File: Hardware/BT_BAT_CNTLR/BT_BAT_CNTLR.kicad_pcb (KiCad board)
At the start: 2 copper layers, 145 x 60 mm, 10 parts, among them J1 Barrel_Jack_Switch

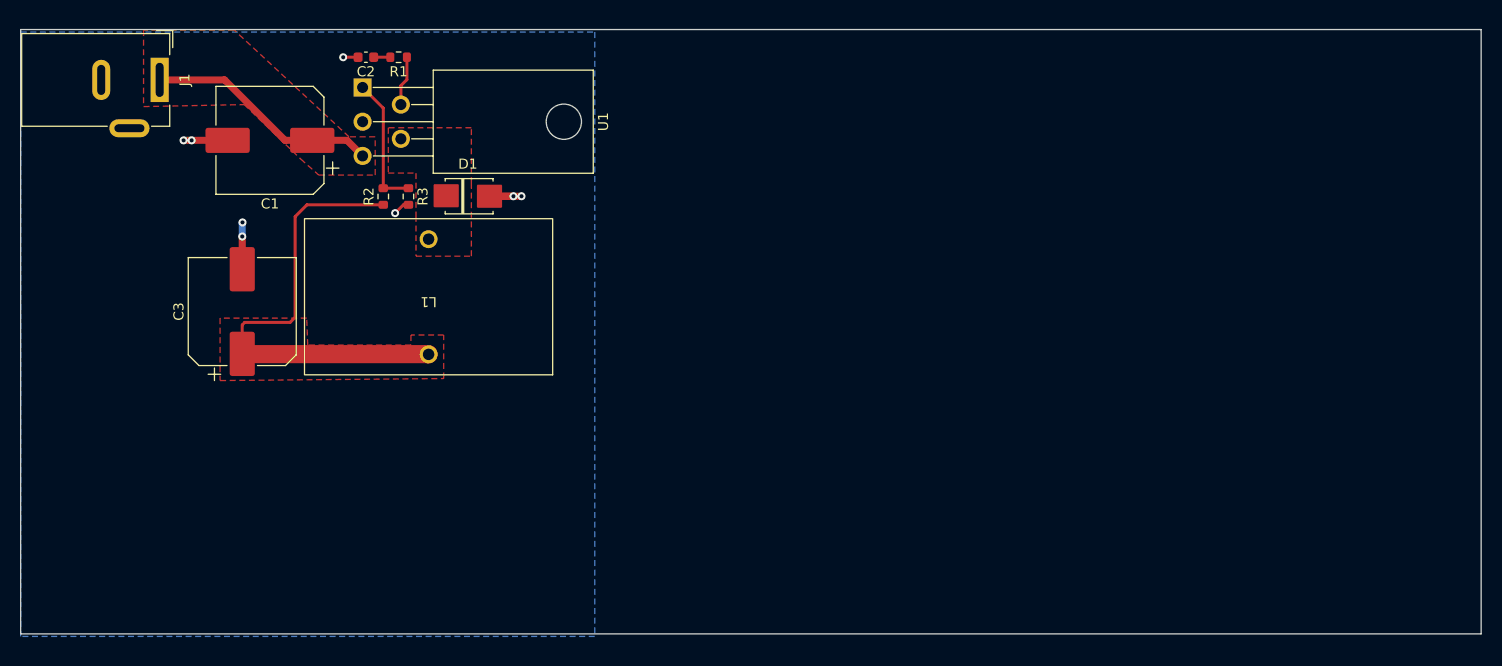
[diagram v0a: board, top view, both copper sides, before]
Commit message: dead ass think I just added a second copy..
aight. routed caps and antenna for nRF.
need to route power and find a new IC for USB ports.
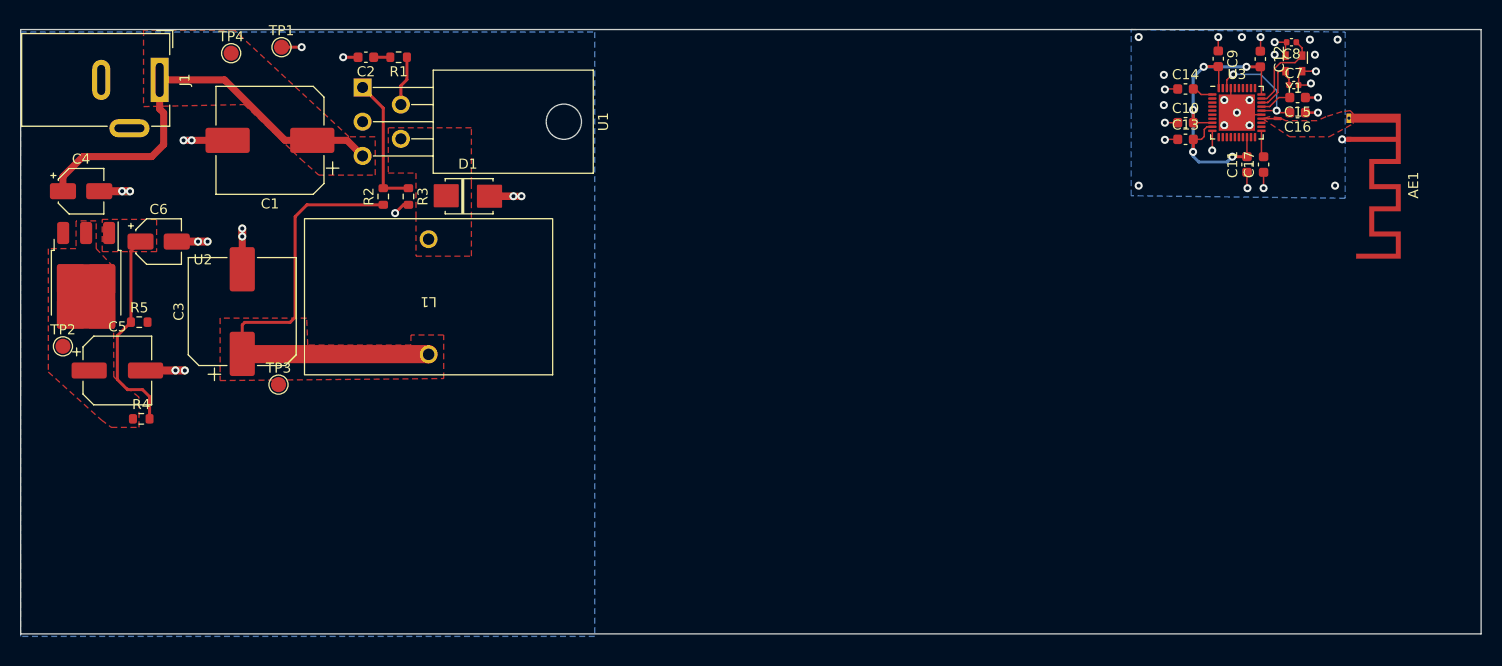
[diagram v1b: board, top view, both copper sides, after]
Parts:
- added AE1: Antenna_Chip, RF_Antenna:Texas_SWRA117D_2.4GHz_Right, F.Cu at (172.9, 44.6)
- added C10: 4.7uF, Capacitor_SMD:C_0603_1608Metric, F.Cu at (156.7, 43.0)
- added C11: 100nF, Capacitor_SMD:C_0603_1608Metric, F.Cu at (162.8, 47.1)
- added C12: 100nF, Capacitor_SMD:C_0603_1608Metric, F.Cu at (164.1, 36.7)
- added C13: 4.7uF, Capacitor_SMD:C_0603_1608Metric, F.Cu at (156.7, 44.6)
- added C14: 01.uF, Capacitor_SMD:C_0603_1608Metric, F.Cu at (156.7, 39.6)
- added C15: 100pF, Capacitor_SMD:C_0603_1608Metric, F.Cu at (167.8, 40.5)
- added C16: 1uF, Capacitor_SMD:C_0603_1608Metric, F.Cu at (167.8, 42.0)
- added C17: 820pF, Capacitor_SMD:C_0603_1608Metric, F.Cu at (164.4, 47.1)
- added C4: 10uF, Capacitor_SMD:CP_Elec_4x4.5, F.Cu at (47.0, 49.8)
- added C5: 100uF, Capacitor_SMD:CP_Elec_6.3x5.2, F.Cu at (50.6, 67.6)
- added C6: 10uF, Capacitor_SMD:CP_Elec_4x4.5, F.Cu at (54.7, 54.8)
- added C7: 20pF, Capacitor_SMD:C_0402_1005Metric, F.Cu at (167.4, 39.3)
- added C8: 20pF, Capacitor_SMD:C_0402_1005Metric, F.Cu at (167.2, 35.0)
- added C9: 1.0uF, Capacitor_SMD:C_0603_1608Metric, F.Cu at (159.9, 36.6)
- added R4: 6.04k, Resistor_SMD:R_0603_1608Metric, F.Cu at (53.0, 72.4)
- added R5: 10k, Resistor_SMD:R_0603_1608Metric, F.Cu at (52.8, 62.8)
- added TP1: TestPoint, TestPoint:TestPoint_Pad_D1.5mm, F.Cu at (66.9, 35.5)
- added TP2: TestPoint, TestPoint:TestPoint_Pad_D1.5mm, F.Cu at (45.2, 65.2)
- added TP3: TestPoint, TestPoint:TestPoint_Pad_D1.5mm, F.Cu at (66.6, 69.0)
- added TP4: TestPoint, TestPoint:TestPoint_Pad_D1.5mm, F.Cu at (61.9, 36.1)
- added U2: LM1117DT-ADJ, Package_TO_SOT_SMD:TO-252-3_TabPin2, F.Cu at (47.5, 59.0)
- added U3: nRF52820-QDxx, Package_DFN_QFN:QFN-40-1EP_5x5mm_P0.4mm_EP3.6x3.6mm, F.Cu at (161.8, 42.0)
- added Y1: Crystal_GND24, Oscillator:Oscillator_SMD_Abracon_ASDMB-4Pin_2.5x2.0mm, F.Cu at (167.4, 37.1)
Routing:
- net GND: track 20.1 -> 59.4 mm, vias 8 -> 44
- net +3V3: track 0.00 -> 35.7 mm, vias 0 -> 5
- net /Power/adj: track 0.00 -> 20.8 mm
- net VIN: track 23.3 -> 42.6 mm
- net Net-(U3-DEC4): track 0.00 -> 11.5 mm, vias 0 -> 2
- net Net-(U3-XC2): track 0.00 -> 8.66 mm
- net Net-(U3-XC1): track 0.00 -> 6.36 mm
- net Net-(U3-DEC3): track 0.00 -> 3.19 mm
- net Net-(U3-DEC5): track 0.00 -> 2.66 mm
- net /uC/ANT: track 0.00 -> 1.90 mm
- net Net-(U3-DEC1): track 0.00 -> 1.89 mm
- added copper zone on F.Cu, net +3V3
- added copper zone on F.Cu, net /Power/adj
- added copper zone on F.Cu, net /uC/ANT

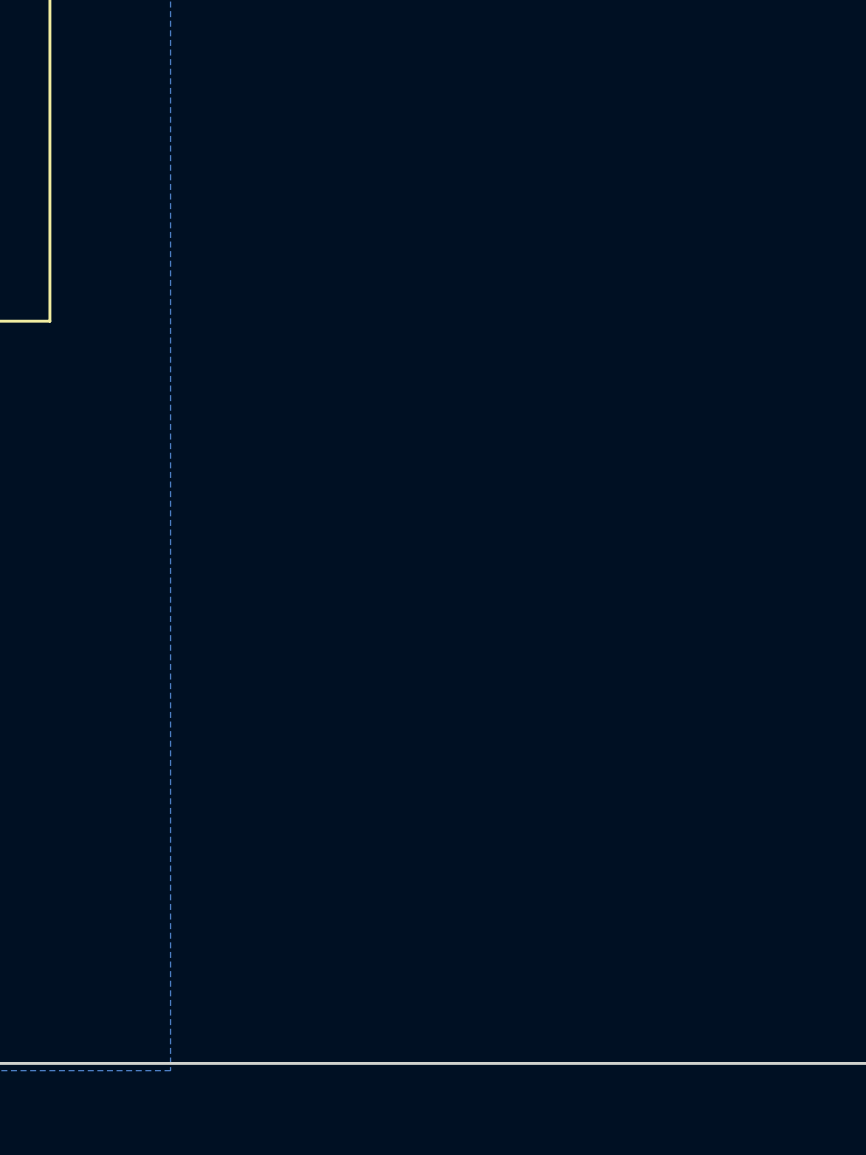
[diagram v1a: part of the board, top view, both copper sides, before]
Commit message: Added 1 USB circuit
will wait for approval/ review before continuing
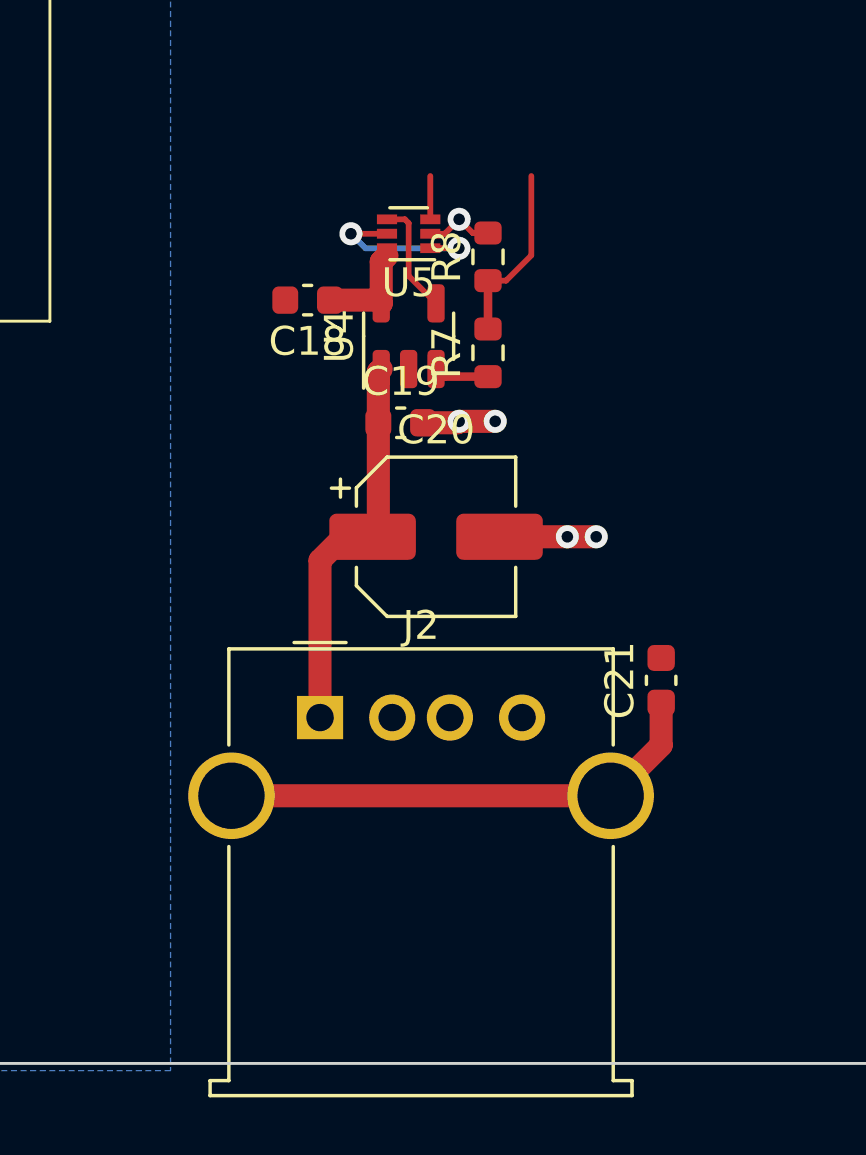
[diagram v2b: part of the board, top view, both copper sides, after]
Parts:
- added C18: 1uF, Capacitor_SMD:C_0603_1608Metric, F.Cu at (102.8, 67.3)
- added C19: 0.1uF, Capacitor_SMD:C_0603_1608Metric, F.Cu at (106.0, 71.5)
- added C20: 120uF, Capacitor_SMD:CP_Elec_5x5.9, F.Cu at (107.2, 75.5)
- added C21: 10nF, Capacitor_SMD:C_0603_1608Metric, F.Cu at (115.0, 80.5)
- added J2: USB_A, Connector_USB:USB_A_Molex_67643_Horizontal, F.Cu at (103.2, 81.8)
- added R7: 1.1k, Resistor_SMD:R_0603_1608Metric, F.Cu at (109.0, 69.1)
- added R8: 2.2k, Resistor_SMD:R_0603_1608Metric, F.Cu at (109.0, 65.8)
- added U4: AP22814AW5, Package_TO_SOT_SMD:SOT-23-5, F.Cu at (106.2, 68.5)
- added U5: SN74LVC1T45DRL, Package_TO_SOT_SMD:SOT-563, F.Cu at (106.2, 65.0)
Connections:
- U3 pad 14: unconnected-(U3-P0.14-Pad14) -> /uC/FLT_4
- U3 pad 15: unconnected-(U3-P0.15-Pad15) -> /uC/FLT_5
- U3 pad 2: unconnected-(U3-XL1/P0.00-Pad2) -> /USB connectors+load switches/EN_1
- U3 pad 22: unconnected-(U3-P0.16-Pad22) -> /uC/FLT_6
- U3 pad 3: unconnected-(U3-XL2/P0.01-Pad3) -> /uC/EN_2
- U3 pad 31: unconnected-(U3-P0.08-Pad31) -> /uC/FLT_3
- U3 pad 35: unconnected-(U3-AIN1/P0.03-Pad35) -> /uC/EN_4
- U3 pad 36: unconnected-(U3-AIN0/P0.02-Pad36) -> /uC/EN_3
- U3 pad 4: unconnected-(U3-AIN2/P0.04-Pad4) -> /uC/EN_5
- U3 pad 5: unconnected-(U3-AIN3/P0.05-Pad5) -> /uC/EN_6
- U3 pad 6: unconnected-(U3-P0.06-Pad6) -> /uC/FLT_1
- U3 pad 7: unconnected-(U3-P0.07-Pad7) -> /uC/FLT_2
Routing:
- net Net-(J2-Shield): track 0.00 -> 17.1 mm
- net Net-(J2-VBUS): track 0.00 -> 13.5 mm
- net GND: track 59.4 -> 67.7 mm, vias 44 -> 49
- net FLT_1: track 0.00 -> 6.29 mm
- net +3V3: track 35.7 -> 41.8 mm, vias 5 -> 7
- net /USB connectors+load switches/EN1: track 0.00 -> 3.98 mm
- net 5V_5A: track 46.3 -> 49.8 mm
- net Net-(U4-~{FLG}): track 0.00 -> 1.91 mm
- net /USB connectors+load switches/EN_1: track 0.00 -> 1.50 mm

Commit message: - Github Tree Cleanup - Power Routing
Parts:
- added C22: 1uF, Capacitor_SMD:C_0603_1608Metric, F.Cu at (115.5, 70.1)
- added C23: 0.1uF, Capacitor_SMD:C_0603_1608Metric, F.Cu at (116.4, 75.8)
- added C24: 120uF, Capacitor_SMD:CP_Elec_5x5.9, F.Cu at (122.3, 75.8)
- added C25: 10nF, Capacitor_SMD:C_0603_1608Metric, F.Cu at (132.2, 80.8)
- added C26: 1uF, Capacitor_SMD:C_0603_1608Metric, F.Cu at (80.2, 70.5)
- added C27: 0.1uF, Capacitor_SMD:C_0603_1608Metric, F.Cu at (81.5, 75.2)
- added C28: 120uF, Capacitor_SMD:CP_Elec_5x5.9, F.Cu at (87.2, 75.8)
- added C29: 10nF, Capacitor_SMD:C_0603_1608Metric, F.Cu at (96.5, 80.5)
- added C30: 1uF, Capacitor_SMD:C_0603_1608Metric, F.Cu at (168.0, 69.6)
- added C31: 0.1uF, Capacitor_SMD:C_0603_1608Metric, F.Cu at (168.9, 75.5)
- added C32: 120uF, Capacitor_SMD:CP_Elec_5x5.9, F.Cu at (174.9, 75.5)
- added C33: 10nF, Capacitor_SMD:C_0603_1608Metric, F.Cu at (184.4, 80.4)
- added C34: 1uF, Capacitor_SMD:C_0603_1608Metric, F.Cu at (150.3, 69.9)
- added C35: 0.1uF, Capacitor_SMD:C_0603_1608Metric, F.Cu at (151.5, 75.5)
- added C36: 120uF, Capacitor_SMD:CP_Elec_5x5.9, F.Cu at (157.2, 75.5)
- added C37: 10nF, Capacitor_SMD:C_0603_1608Metric, F.Cu at (166.5, 80.5)
- added C38: 1uF, Capacitor_SMD:C_0603_1608Metric, F.Cu at (132.8, 70.1)
- added C39: 0.1uF, Capacitor_SMD:C_0603_1608Metric, F.Cu at (133.8, 75.8)
- added C40: 120uF, Capacitor_SMD:CP_Elec_5x5.9, F.Cu at (139.6, 75.8)
- added C41: 10nF, Capacitor_SMD:C_0603_1608Metric, F.Cu at (149.3, 80.5)
- added J3: USB_A, Connector_USB:USB_A_Molex_67643_Horizontal, F.Cu at (120.0, 81.6)
- added J4: USB_A, Connector_USB:USB_A_Molex_67643_Horizontal, F.Cu at (85.0, 81.6)
- added J5: USB_A, Connector_USB:USB_A_Molex_67643_Horizontal, F.Cu at (172.5, 81.6)
- added J6: USB_A, Connector_USB:USB_A_Molex_67643_Horizontal, F.Cu at (155.0, 81.6)
- added J7: USB_A, Connector_USB:USB_A_Molex_67643_Horizontal, F.Cu at (137.5, 81.6)
- added J8: Conn_ARM_SWD_TagConnect_TC2030, Connector:Tag-Connect_TC2030-IDC-FP_2x03_P1.27mm_Vertical, F.Cu at (161.2, 57.3)
- added R10: 1.1k, Resistor_SMD:R_0603_1608Metric, F.Cu at (85.8, 71.1)
- added R11: 2.2k, Resistor_SMD:R_0603_1608Metric, F.Cu at (87.5, 71.1)
- added R12: 1.1k, Resistor_SMD:R_0603_1608Metric, F.Cu at (173.4, 70.6)
- added R13: 2.2k, Resistor_SMD:R_0603_1608Metric, F.Cu at (174.9, 70.6)
- added R14: 1.1k, Resistor_SMD:R_0603_1608Metric, F.Cu at (155.8, 70.8)
- added R15: 2.2k, Resistor_SMD:R_0603_1608Metric, F.Cu at (157.2, 70.8)
- added R16: 1.1k, Resistor_SMD:R_0603_1608Metric, F.Cu at (138.3, 71.1)
- added R17: 2.2k, Resistor_SMD:R_0603_1608Metric, F.Cu at (139.8, 71.1)
- added R6: 1.1k, Resistor_SMD:R_0603_1608Metric, F.Cu at (120.8, 71.2)
- added R9: 2.2k, Resistor_SMD:R_0603_1608Metric, F.Cu at (122.3, 71.2)
- added U10: SN74LVC1T45DRL, Package_TO_SOT_SMD:SOT-563, F.Cu at (141.9, 46.8)
- added U11: AP22814AW5, Package_TO_SOT_SMD:SOT-23-5, F.Cu at (170.7, 70.1)
- added U12: SN74LVC1T45DRL, Package_TO_SOT_SMD:SOT-563, F.Cu at (135.0, 46.8)
- added U13: AP22814AW5, Package_TO_SOT_SMD:SOT-23-5, F.Cu at (153.1, 70.4)
- added U14: SN74LVC1T45DRL, Package_TO_SOT_SMD:SOT-563, F.Cu at (129.6, 47.0)
- added U15: AP22814AW5, Package_TO_SOT_SMD:SOT-23-5, F.Cu at (135.6, 70.6)
- added U6: SN74LVC1T45DRL, Package_TO_SOT_SMD:SOT-563, F.Cu at (141.2, 38.8)
- added U7: AP22814AW5, Package_TO_SOT_SMD:SOT-23-5, F.Cu at (118.1, 70.7)
- added U8: SN74LVC1T45DRL, Package_TO_SOT_SMD:SOT-563, F.Cu at (129.6, 38.9)
- added U9: AP22814AW5, Package_TO_SOT_SMD:SOT-23-5, F.Cu at (83.0, 70.8)
- moved U5 38.7 mm to (134.7, 38.8)
- moved C19 7.97 mm to (99.0, 75.5), turned to 180 degrees
- moved R8 6.56 mm to (105.0, 71.0), turned to -90 degrees
- moved U4 5.84 mm to (100.8, 70.5)
- moved R7 5.81 mm to (103.5, 71.0)
- moved C18 5.48 mm to (98.0, 70.0), turned to -90 degrees
- moved C20 2.41 mm to (104.8, 75.8)
- moved C17 1.44 mm to (165.8, 46.8)
- moved C10 1.12 mm to (156.7, 44.1)
- moved C13 1.12 mm to (156.7, 45.8)
- moved J2 0.69 mm to (102.5, 81.6)
- moved AE1 0.44 mm to (172.9, 45.1)
- moved C11 0.44 mm to (162.8, 47.6)
- moved C12 0.44 mm to (164.1, 37.1)
- moved C8 0.44 mm to (167.2, 35.4)
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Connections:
- R7 pad 2: FLT_1 -> /USB connectors+load switches/FLT_1
- R8 pad 1: FLT_1 -> /USB connectors+load switches/FLT_1
- U3 pad 14: /uC/FLT_4 -> /USB connectors+load switches/FLT_4
- U3 pad 15: /uC/FLT_5 -> /USB connectors+load switches/FLT_5
- U3 pad 16: unconnected-(U3-P0.18/~{RESET}-Pad16) -> /uC/RESET
- U3 pad 19: unconnected-(U3-SWDIO-Pad19) -> /uC/SWDIO
- U3 pad 20: unconnected-(U3-SWDCLK-Pad20) -> /uC/SWDCLK
- U3 pad 22: /uC/FLT_6 -> /USB connectors+load switches/FLT_6
- U3 pad 3: /uC/EN_2 -> /USB connectors+load switches/EN_2
- U3 pad 31: /uC/FLT_3 -> /USB connectors+load switches/FLT_3
- U3 pad 35: /uC/EN_4 -> /USB connectors+load switches/EN_4
- U3 pad 36: /uC/EN_3 -> /USB connectors+load switches/EN_3
- U3 pad 4: /uC/EN_5 -> /USB connectors+load switches/EN_5
- U3 pad 5: /uC/EN_6 -> /USB connectors+load switches/EN_6
- U3 pad 6: /uC/FLT_1 -> /USB connectors+load switches/FLT_1
- U3 pad 7: /uC/FLT_2 -> /USB connectors+load switches/FLT_2
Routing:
- net +3V3: track 41.8 -> 178.8 mm, vias 7 -> 22
- net /USB connectors+load switches/FLT_3: track 0.00 -> 104.1 mm, vias 0 -> 4
- net /USB connectors+load switches/FLT_1: track 0.00 -> 71.9 mm, vias 0 -> 2
- net /USB connectors+load switches/EN3: track 0.00 -> 58.2 mm
- net /USB connectors+load switches/FLT_2: track 0.00 -> 55.1 mm, vias 0 -> 2
- net /USB connectors+load switches/EN6: track 0.00 -> 49.1 mm
- net GND: track 67.7 -> 112.1 mm, vias 49 -> 74
- net /USB connectors+load switches/EN2: track 0.00 -> 43.7 mm
- net /USB connectors+load switches/EN_4: track 0.00 -> 42.4 mm, vias 0 -> 2
- net /USB connectors+load switches/EN1: track 3.98 -> 46.1 mm
- net /USB connectors+load switches/EN_3: track 0.00 -> 38.9 mm, vias 0 -> 2
- net /USB connectors+load switches/FLT_4: track 0.00 -> 37.4 mm, vias 0 -> 2
- net /USB connectors+load switches/EN5: track 0.00 -> 35.8 mm
- net /USB connectors+load switches/FLT_6: track 0.00 -> 31.8 mm
- net /USB connectors+load switches/FLT_5: track 0.00 -> 29.0 mm, vias 0 -> 2
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- added copper zone on B.Cu, net +3V3
- added copper zone on B.Cu, net 5V_5A
- added copper zone on F.Cu, net GND

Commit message: Need Help
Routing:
- net 5V_5A: track 77.8 -> 150.7 mm
- net +3V3: track 178.8 -> 222.9 mm, vias 22 -> 28
- net GND: track 112.1 -> 120.6 mm, vias 74 -> 82
- net Net-(J7-Shield): track 17.0 -> 18.6 mm
- net Net-(J6-Shield): track 16.8 -> 18.5 mm
- net Net-(J5-Shield): track 17.0 -> 18.7 mm
- net Net-(J4-Shield): track 16.8 -> 18.4 mm
- net Net-(J3-Shield): track 16.8 -> 18.5 mm
- net Net-(J2-Shield): track 17.2 -> 18.9 mm
